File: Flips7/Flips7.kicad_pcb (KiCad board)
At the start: 2 copper layers, 100 x 100 mm, 16 parts, among them CN1 Conn_02x16_Odd_Even, CN2 Conn_02x16_Odd_Even, U1 FP2800A, U2 FP2800A, U3 FP2800A

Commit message: new routing attempt (wip) for Flips7
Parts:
- BOARD1: footprint IDC_Numbering_Pin_Header_Straight_2x30_Pitch2.54mm -> Own:Pin_Header_Straight_Shrouded_2x30_Pitch2.54mm_AltNumbering
- CN1, CN2: value Conn_02x16_Odd_Even -> Conn_02x17_Odd_Even; footprint Pin_Headers:Pin_Header_Straight_2x16_Pitch2.54mm -> Own:Pin_Header_Straight_Shrouded_2x17_Pitch2.54mm_ConvNumbering
- CNX1, CNY1, CNY2: footprint Own:Pin_Header_Angle_Shrouded_2x05_Pitch2.54mm -> Own:Pin_Header_Angle_Shrouded_2x05_Pitch2.54mm_ConvNumbering
- moved REF** 121.8 mm to (247.7, 191.8)
- moved REF*** 121.8 mm to (261.6, 188.0)
- moved REF*** 121.8 mm to (176.5, 189.2)
- moved CN2 94.9 mm to (41.9, 102.9), turned to 180 degrees
- moved C1 82.3 mm to (158.1, 140.3)
- moved U2 70.0 mm to (82.5, 64.8)
- moved CNY2 69.6 mm to (95.2, 119.4)
- moved BOARD1 63.5 mm to (39.4, 31.8)
- moved CN1 61.6 mm to (31.8, 102.9), turned to 180 degrees
- moved C3 39.5 mm to (157.5, 134.6)
- moved U1 30.1 mm to (58.4, 64.8)
- moved CNY1 29.0 mm to (71.1, 119.4)
- moved U3 27.7 mm to (106.7, 64.8)
- moved CNX1 26.5 mm to (119.4, 119.4)
- moved JP1 19.4 mm to (156.2, 119.4)
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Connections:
- CN1 pad 10: /RY05 -> /RY13
- CN1 pad 11: /~SY06 -> /~SY05
- CN1 pad 12: /RY06 -> /RY12
- CN1 pad 14: /RY07 -> /RY14
- CN1 pad 15: /~SY08 -> /~SY14
- CN1 pad 16: /RY08 -> /RY07
- CN1 pad 17: /~SY09 -> /~SY12
- CN1 pad 18: /RY09 -> /RY05
- CN1 pad 19: /~SY10 -> Net-(CN1-Pad19)
- CN1 pad 2: /RY01 -> /RY08
- CN1 pad 20: /RY10 -> Net-(CN1-Pad20)
- CN1 pad 21: /~SY11 -> /~SY08
- CN1 pad 22: /RY11 -> /RY01
- CN1 pad 23: /~SY12 -> /~SY09
- CN1 pad 24: /RY12 -> /RY02
- CN1 pad 25: /~SY13 -> /~SY10
- CN1 pad 26: /RY13 -> /RY03
- CN1 pad 27: /~SY14 -> /~SY13
- CN1 pad 28: /RY14 -> /RY06
- CN1 pad 29: /~SY15 -> /~SY11
- CN1 pad 30: /RY15 -> /RY04
- CN1 pad 31: /~SY16 -> /~SY15
- CN1 pad 32: /RY16 -> /RY15
- CN1 pad 4: /RY02 -> /RY09
- CN1 pad 6: /RY03 -> /RY10
- CN1 pad 8: /RY04 -> /RY11
- CN1 pad 9: /~SY05 -> /~SY06
- CN2 pad 10: /RY05 -> /RY13
- CN2 pad 11: /~SY06 -> /~SY05
- CN2 pad 12: /RY06 -> /RY12
- CN2 pad 14: /RY07 -> /RY14
- CN2 pad 15: /~SY08 -> /~SY14
- CN2 pad 16: /RY08 -> /RY07
- CN2 pad 17: /~SY09 -> /~SY12
- CN2 pad 18: /RY09 -> /RY05
- CN2 pad 19: /~SY10 -> Net-(CN2-Pad19)
- CN2 pad 2: /RY01 -> /RY08
- CN2 pad 20: /RY10 -> Net-(CN2-Pad20)
- CN2 pad 21: /~SY11 -> /~SY08
- CN2 pad 22: /RY11 -> /RY01
- CN2 pad 23: /~SY12 -> /~SY09
- CN2 pad 24: /RY12 -> /RY02
- CN2 pad 25: /~SY13 -> /~SY10
- CN2 pad 26: /RY13 -> /RY03
- CN2 pad 27: /~SY14 -> /~SY13
- CN2 pad 28: /RY14 -> /RY06
- CN2 pad 29: /~SY15 -> /~SY11
- CN2 pad 30: /RY15 -> /RY04
- CN2 pad 31: /~SY16 -> /~SY15
- CN2 pad 32: /RY16 -> /RY15
- CN2 pad 4: /RY02 -> /RY09
- CN2 pad 6: /RY03 -> /RY10
- CN2 pad 8: /RY04 -> /RY11
- CN2 pad 9: /~SY05 -> /~SY06
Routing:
- net /X02: track 94.2 -> 0.00 mm, vias 3 -> 0
- net /X03: track 90.7 -> 0.00 mm, vias 3 -> 0
- net /X04_NC: track 84.9 -> 0.00 mm, vias 1 -> 0
- net /~SY08: track 178.9 -> 94.8 mm, vias 4 -> 1
- net /~SY11: track 181.7 -> 99.6 mm, vias 3 -> 1
- net /X01: track 80.7 -> 0.00 mm, vias 3 -> 0
- net /~SY05: track 180.1 -> 102.9 mm, vias 4 -> 1
- net /~SY14: track 166.2 -> 89.5 mm, vias 4 -> 1
- net /~SY04: track 175.9 -> 103.3 mm, vias 4 -> 0
- net /RY09: track 205.5 -> 133.0 mm, vias 4 -> 1
- net /RY08: track 194.8 -> 128.3 mm, vias 3 -> 0
- net /RY11: track 192.0 -> 125.7 mm, vias 4 -> 1
- net /~SY13: track 137.7 -> 73.6 mm, vias 4 -> 1
- net /~SY10: track 142.0 -> 79.3 mm, vias 4 -> 1
- net /~SY01: track 172.5 -> 109.9 mm, vias 4 -> 0
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- removed copper zone on B.Cu, net /L.GND
- removed copper zone on B.Cu, net /R.GND
- removed copper zone on B.Cu, net /X.GND
- removed copper zone on F.Cu, net /X.GND
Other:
- net class POW: trace_width 0.3048 -> 0.5

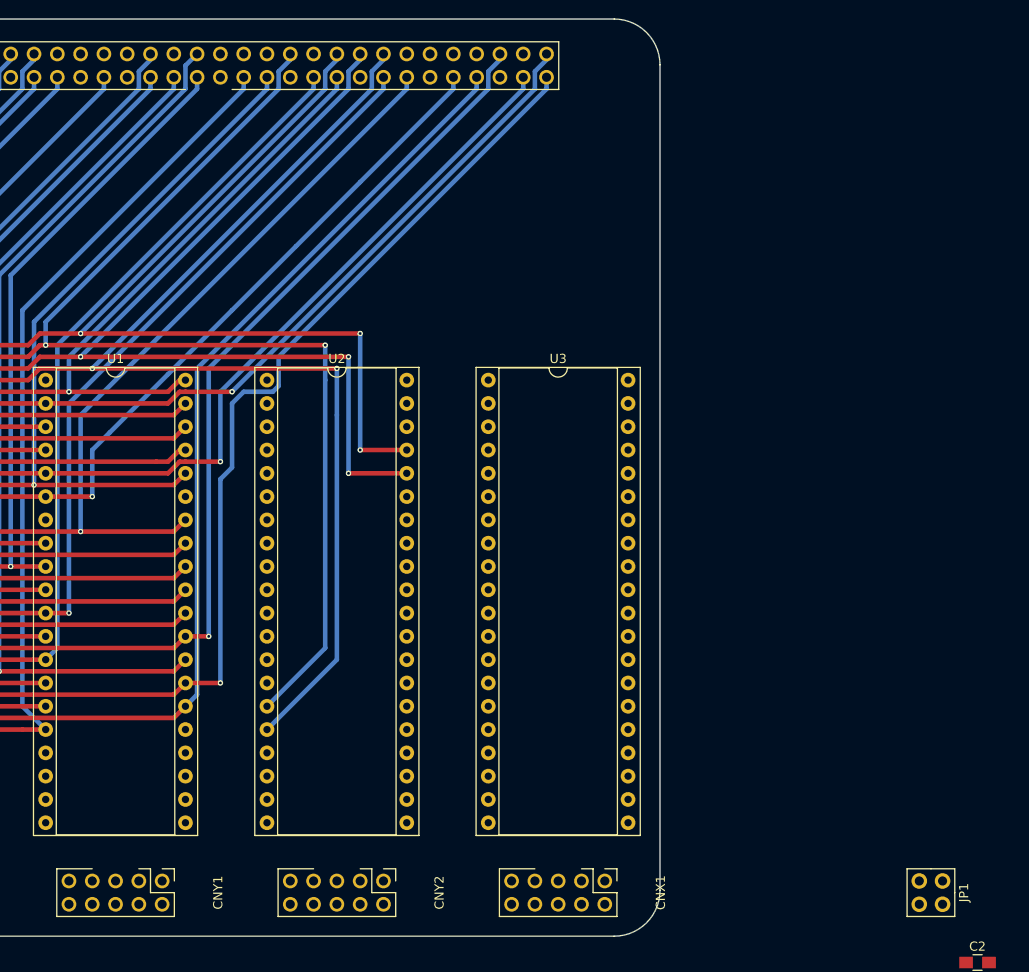
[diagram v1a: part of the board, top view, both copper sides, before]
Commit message: more tracing for Flips7 (still wip)
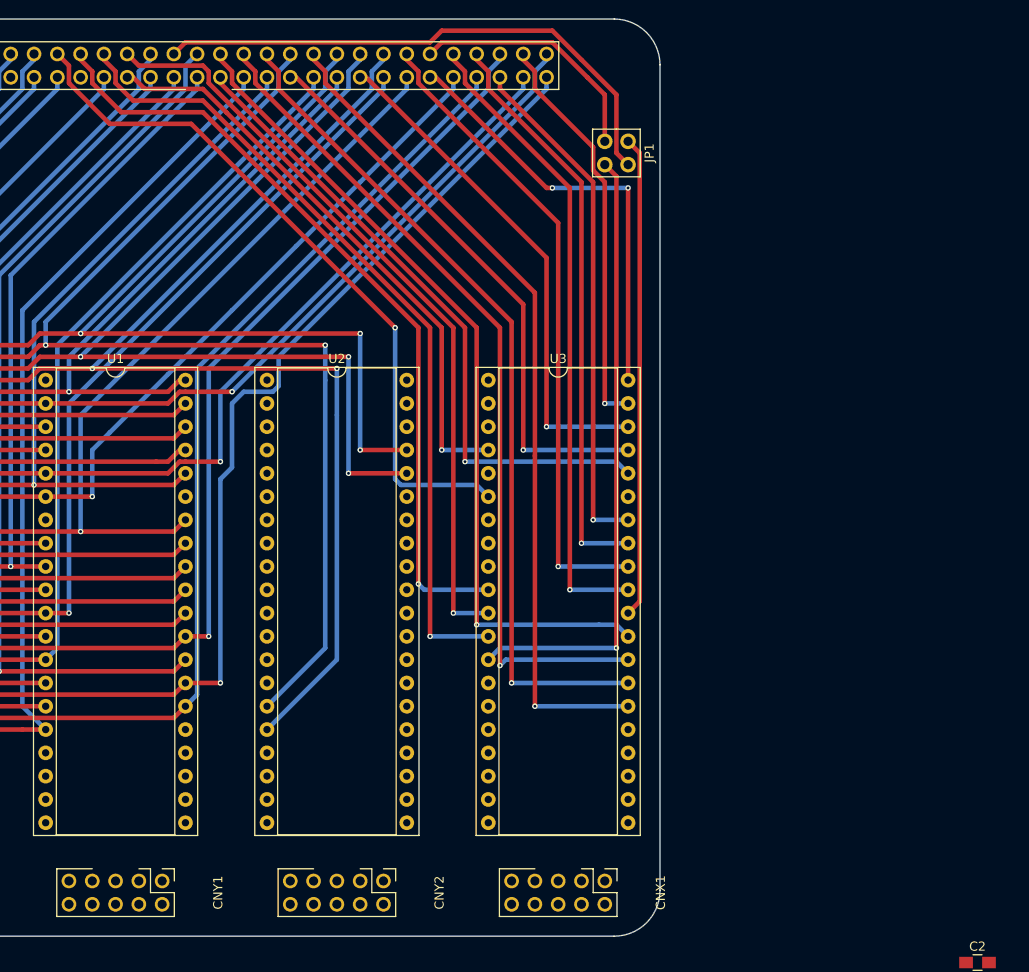
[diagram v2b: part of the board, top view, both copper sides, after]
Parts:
- moved JP1 87.6 mm to (121.9, 38.7)
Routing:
- net /X24: track 0.00 -> 92.5 mm, vias 0 -> 1
- net /X23: track 0.00 -> 92.3 mm, vias 0 -> 1
- net /X22: track 0.00 -> 91.3 mm, vias 0 -> 1
- net /X25: track 0.00 -> 90.8 mm, vias 0 -> 1
- net /X06: track 0.00 -> 89.0 mm, vias 0 -> 1
- net /X07: track 0.00 -> 86.1 mm, vias 0 -> 1
- net /X05: track 0.00 -> 83.6 mm, vias 0 -> 1
- net /X08: track 0.00 -> 77.8 mm, vias 0 -> 1
- net /X15: track 0.00 -> 71.3 mm, vias 0 -> 1
- net /X28: track 0.00 -> 70.3 mm, vias 0 -> 1
- net /X26: track 0.00 -> 70.0 mm, vias 0 -> 1
- net /X04: track 0.00 -> 67.7 mm, vias 0 -> 1
- net /X10: track 0.00 -> 64.0 mm, vias 0 -> 1
- net /X21: track 0.00 -> 63.2 mm, vias 0 -> 1
- net /X16: track 0.00 -> 63.0 mm, vias 0 -> 1
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
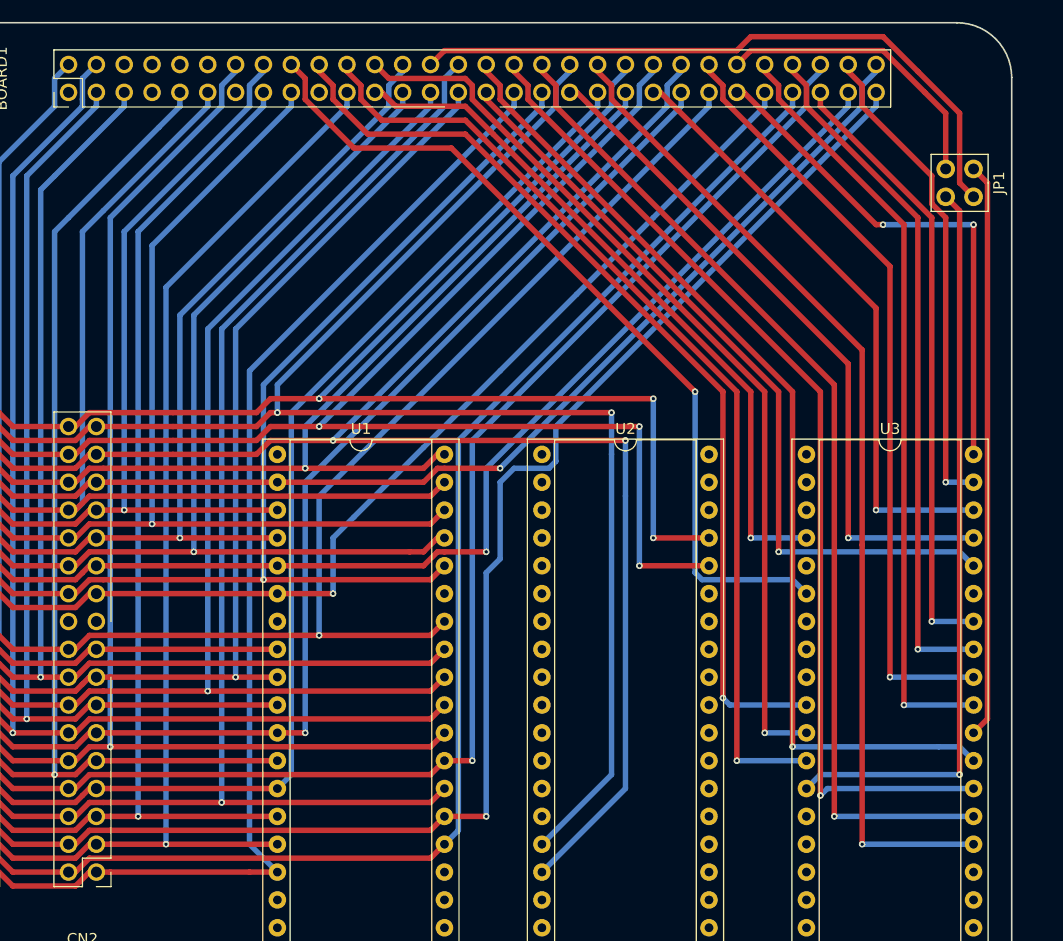
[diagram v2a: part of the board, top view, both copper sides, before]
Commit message: Tracing column driver lines for Flips7
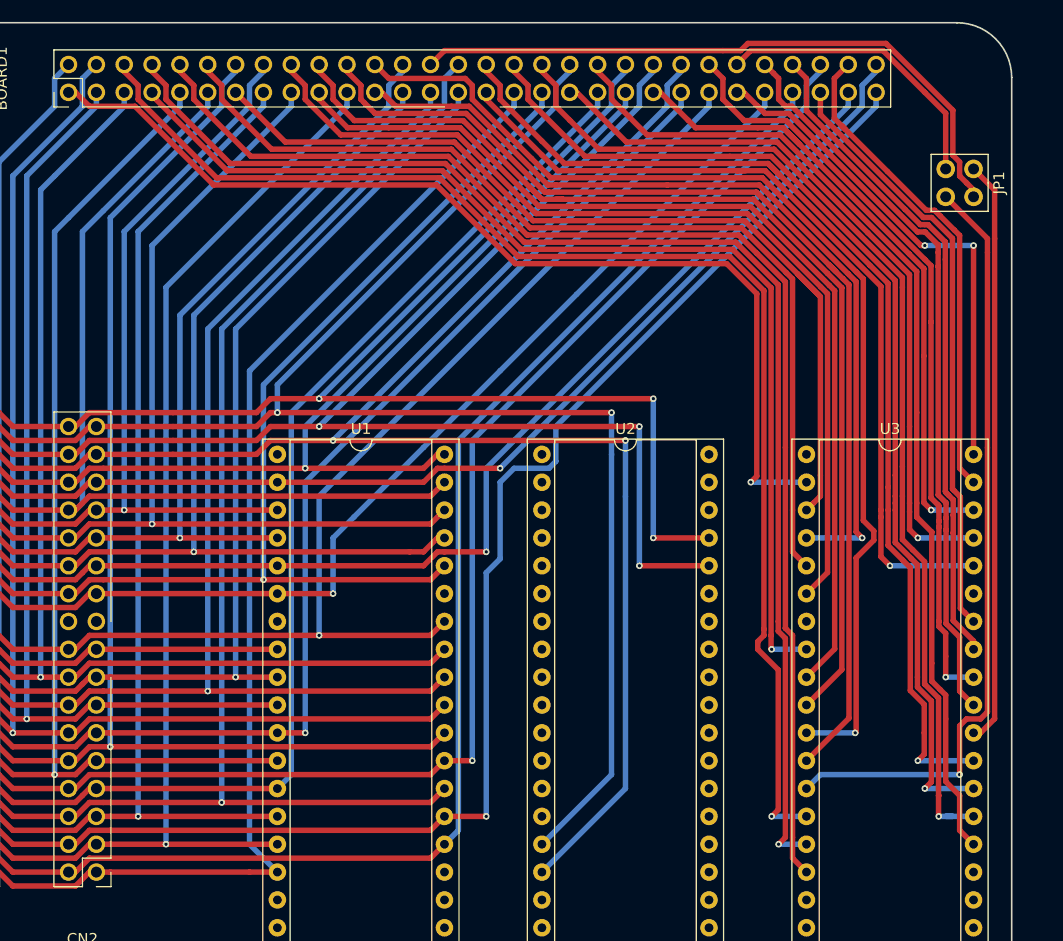
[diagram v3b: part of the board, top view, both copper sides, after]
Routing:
- net /X02: track 0.00 -> 120.6 mm, vias 0 -> 1
- net /X03: track 0.00 -> 120.4 mm, vias 0 -> 1
- net /X01: track 0.00 -> 119.2 mm
- net /X12: track 0.00 -> 100.2 mm, vias 0 -> 1
- net /X11: track 0.00 -> 92.9 mm, vias 0 -> 1
- net /X14: track 0.00 -> 91.2 mm
- net /X09: track 0.00 -> 89.2 mm
- net /X13: track 0.00 -> 84.7 mm
- net /X05: track 83.6 -> 100.3 mm
- net /X10: track 64.0 -> 79.7 mm
- net /X07: track 86.1 -> 98.5 mm, vias 1 -> 0
- net /X06: track 89.0 -> 101.1 mm, vias 1 -> 0
- net /X08: track 77.8 -> 86.8 mm, vias 1 -> 0
- net /X15: track 71.3 -> 77.9 mm
- net /X25: track 90.8 -> 97.5 mm
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
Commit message: Cleanup traces
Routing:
- net /X05: track 100.3 -> 98.4 mm
- net /X02: track 120.6 -> 119.0 mm
- net /X28: track 69.6 -> 68.5 mm
- net /X04: track 70.6 -> 71.5 mm
- net /X10: track 79.7 -> 78.9 mm
- net /X23: track 97.4 -> 96.9 mm

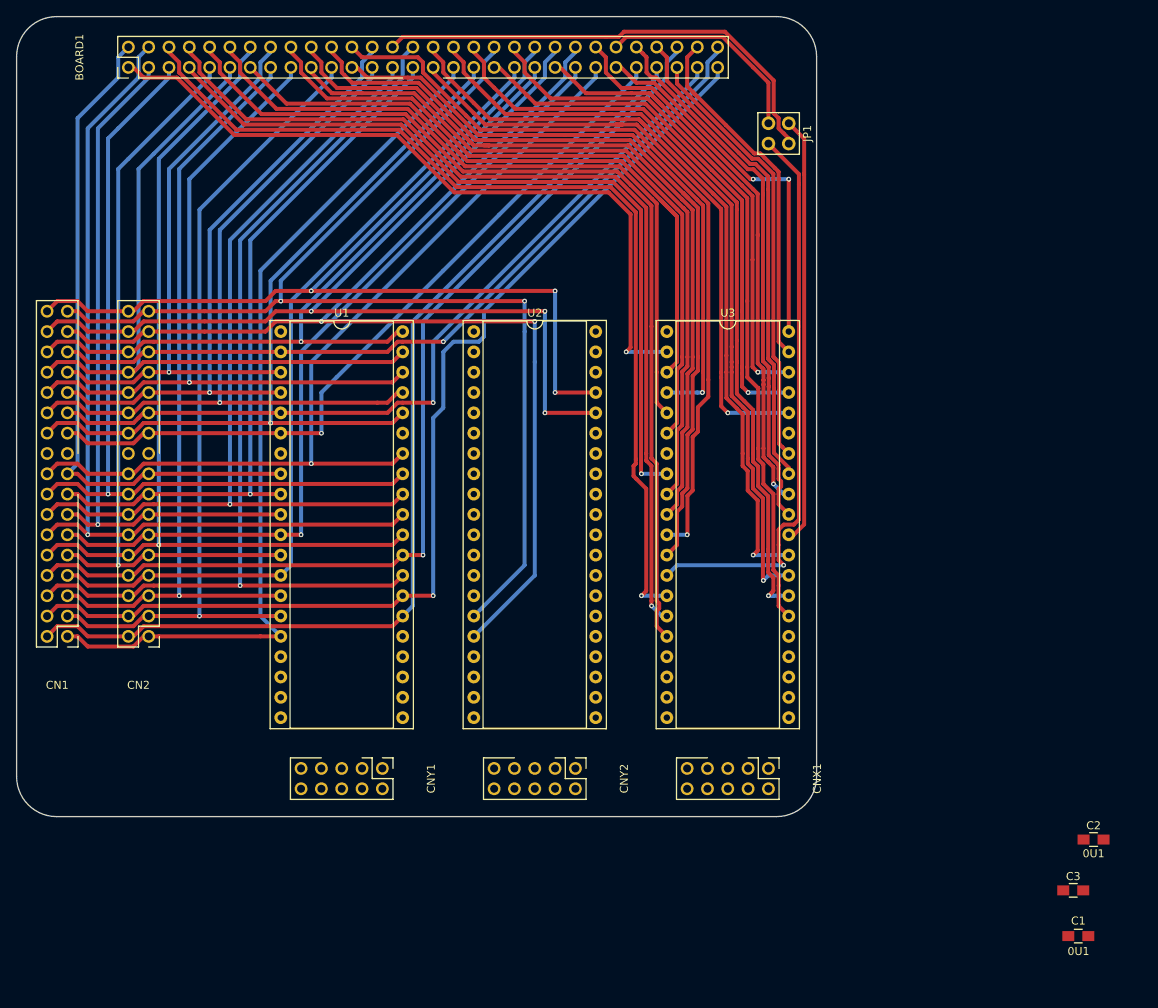
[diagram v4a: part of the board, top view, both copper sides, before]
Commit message: single GND, VCC and HV; almost finish tracing
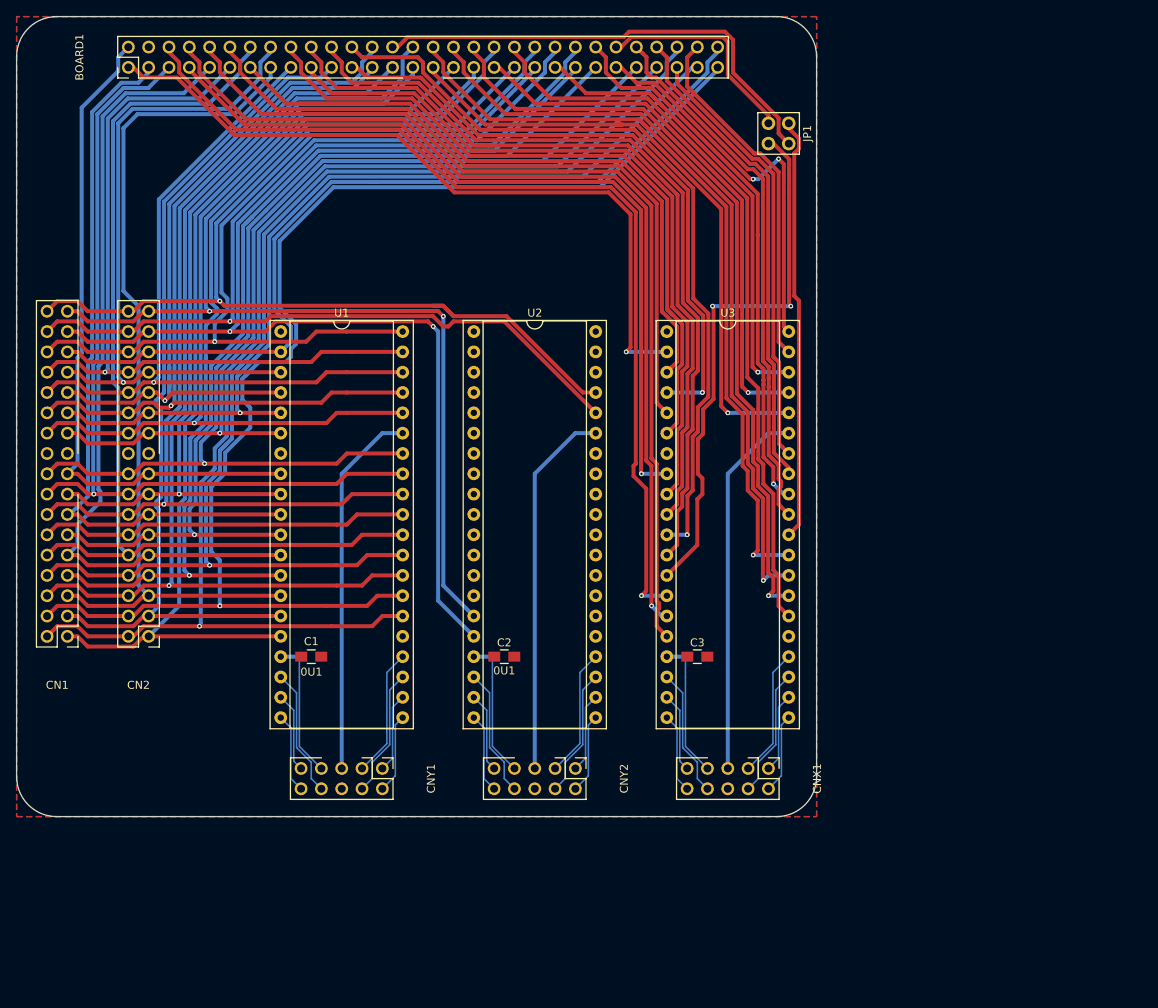
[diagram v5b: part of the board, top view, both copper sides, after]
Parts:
- moved C1 102.0 mm to (62.2, 105.4)
- moved C2 77.1 mm to (86.4, 105.4)
- moved C3 55.3 mm to (110.5, 105.4)
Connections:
- C1 pad 1: /L.GND -> /GND
- C1 pad 2: /L.VCC -> /VCC
- C2 pad 1: /R.VCC -> /VCC
- C2 pad 2: /R.GND -> /GND
- C3 pad 1: /X.VCC -> /VCC
- C3 pad 2: /X.GND -> /GND
- CNX1 pad 5: /X.HV -> /HV
- CNX1 pad 6: /X.GND -> /GND
- CNX1 pad 7: /X.VCC -> /VCC
- CNY1 pad 5: /L.HV -> /HV
- CNY1 pad 6: /L.GND -> /GND
- CNY1 pad 7: /L.VCC -> /VCC
- CNY2 pad 5: /R.HV -> /HV
- CNY2 pad 6: /R.GND -> /GND
- CNY2 pad 7: /R.VCC -> /VCC
- U1 pad 17: /L.VCC -> /VCC
- U1 pad 25: /L.GND -> /GND
- U1 pad 35: /L.HV -> /HV
- U1 pad 7: /L.GND -> /GND
- U2 pad 17: /R.VCC -> /VCC
- U2 pad 25: /R.GND -> /GND
- U2 pad 35: /R.HV -> /HV
- U2 pad 7: /R.GND -> /GND
- U3 pad 17: /X.VCC -> /VCC
- U3 pad 25: /X.GND -> /GND
- U3 pad 35: /X.HV -> /HV
- U3 pad 7: /X.GND -> /GND
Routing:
- net /HV: track 0.00 -> 139.7 mm
- net /RY12: track 110.7 -> 46.6 mm, vias 1 -> 0
- net /VCC: track 0.00 -> 53.2 mm
- net /RY09: track 133.0 -> 165.3 mm
- net /RY11: track 125.7 -> 155.8 mm
- net /RY08: track 128.3 -> 157.1 mm, vias 0 -> 1
- net /RY05: track 110.8 -> 130.5 mm
- net /~SY05: track 102.9 -> 120.5 mm
- net /~SY04: track 103.3 -> 120.8 mm, vias 0 -> 1
- net /RY04: track 92.9 -> 109.6 mm
- net /~SY08: track 94.8 -> 111.1 mm
- net /R.POL: track 0.00 -> 16.1 mm
- net /R.EN: track 0.00 -> 16.1 mm
- net /X.A1: track 0.00 -> 16.1 mm
- net /R.A1: track 0.00 -> 16.1 mm
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- added copper zone on B.Cu, net /GND
- added copper zone on F.Cu, net /GND

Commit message: GND on share connectors
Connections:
- CN1 pad 19: Net-(CN1-Pad19) -> /GND
- CN1 pad 20: Net-(CN1-Pad20) -> /GND
- CN2 pad 19: Net-(CN2-Pad19) -> /GND
- CN2 pad 20: Net-(CN2-Pad20) -> /GND
